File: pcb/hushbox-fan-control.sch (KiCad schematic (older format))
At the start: 23 parts, among them J1 Barrel_Jack_MountingPin, J2 Conn_01x15_Male, M1 Fan_Tacho_PWM, M2 Fan_Tacho_PWM, Q1 IRLML2520, Q2 IRLML2520, SW1 SW_SPST, U1 AMS1117-3.3, U2 ESP32-DevKit-V1, U3 DS18B20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

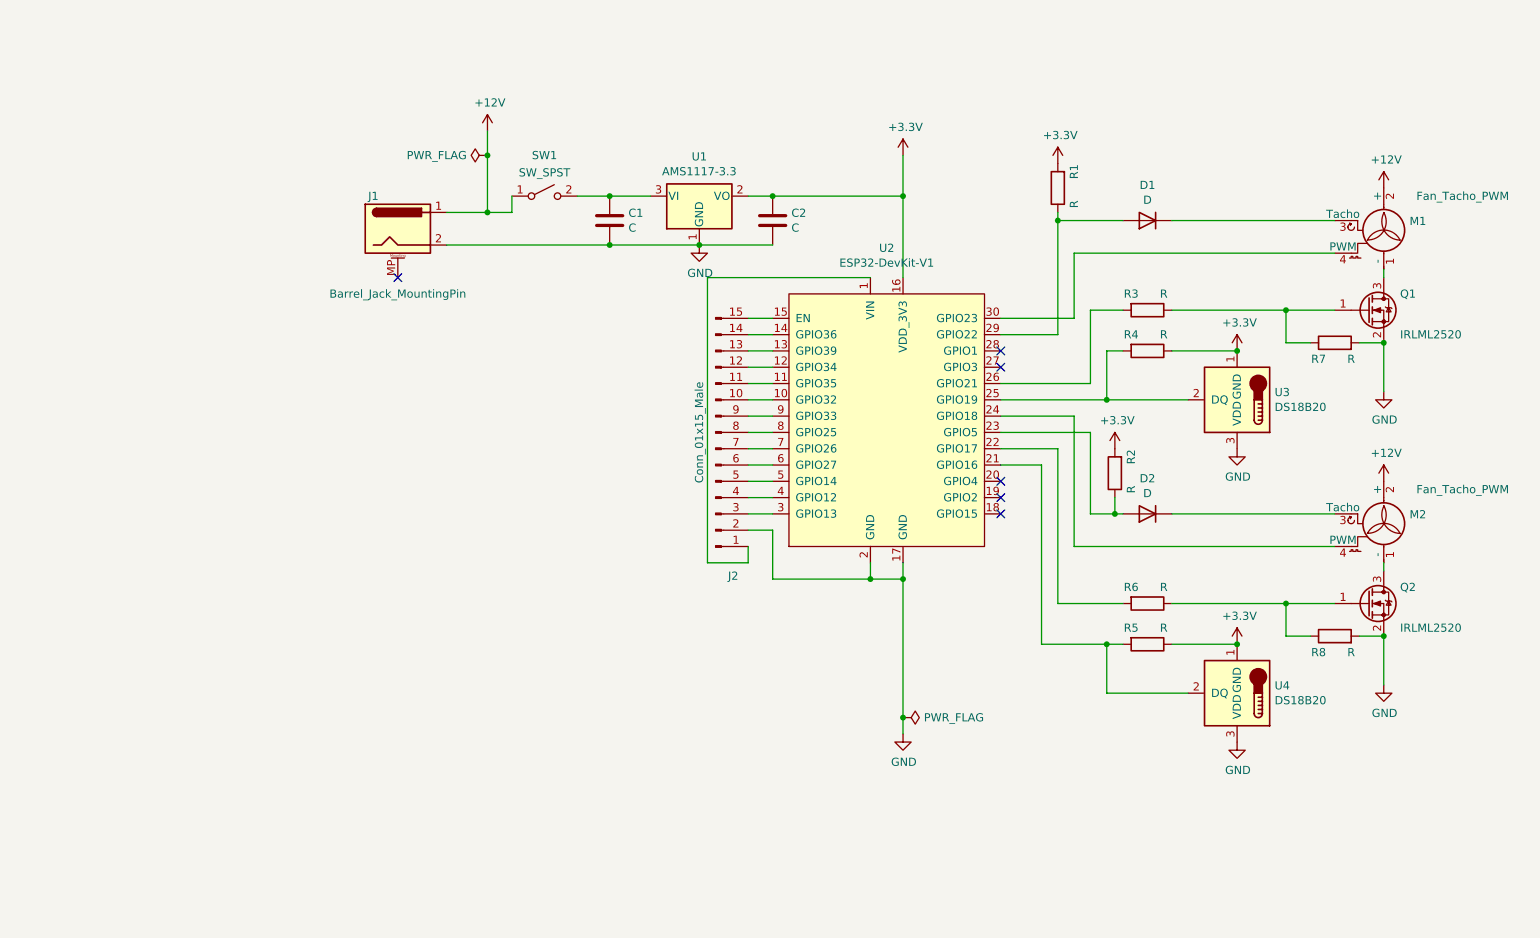
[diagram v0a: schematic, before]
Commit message: improve pcb to v1.1 with IR support
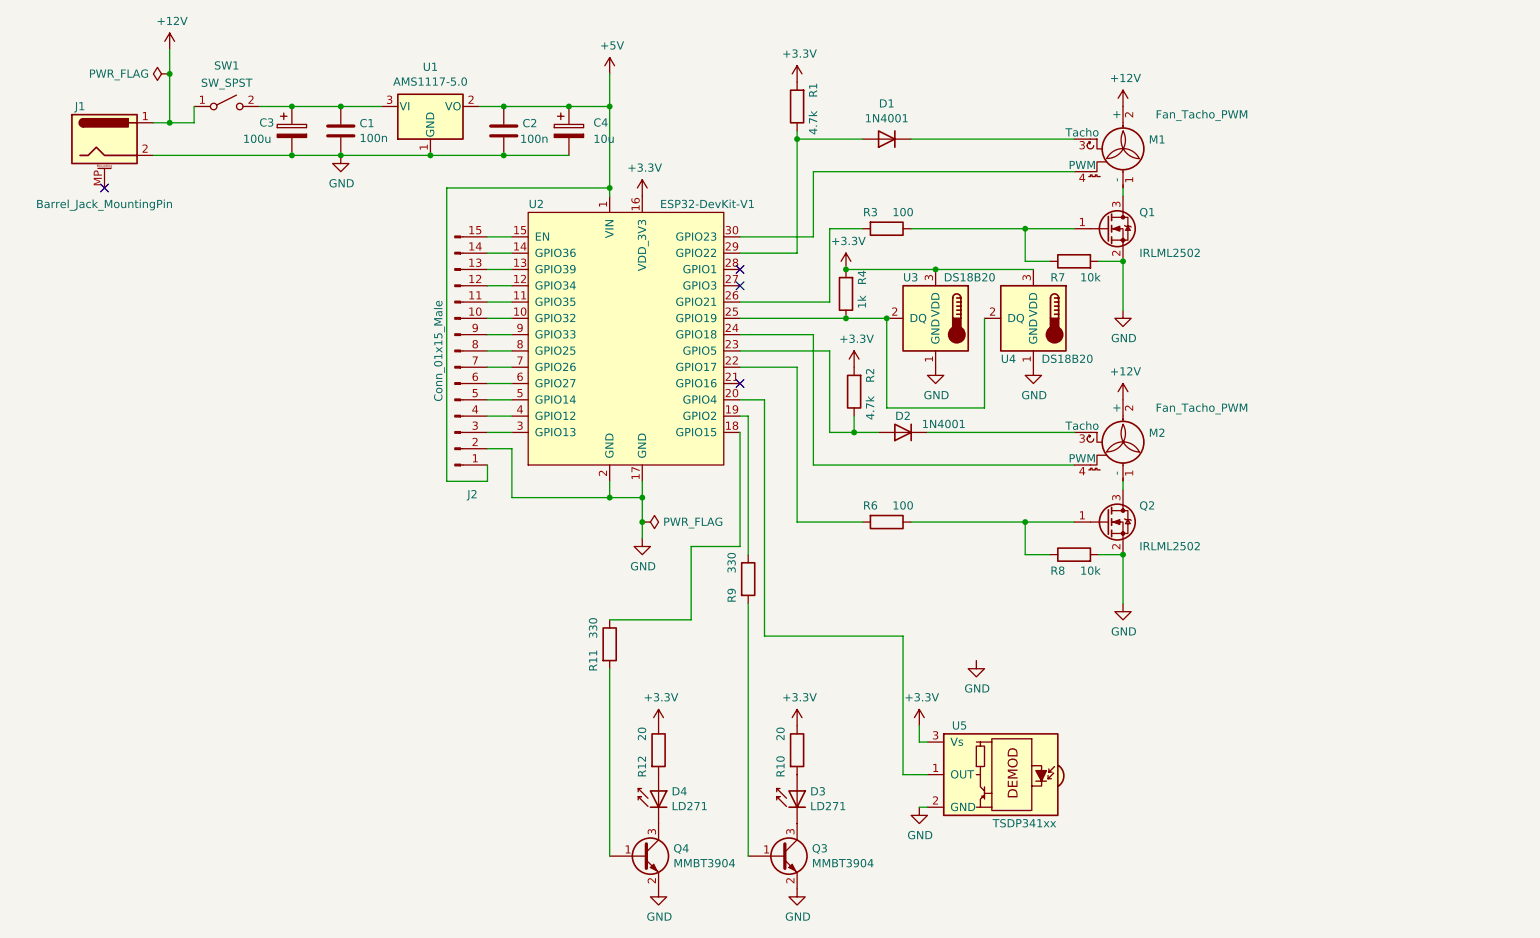
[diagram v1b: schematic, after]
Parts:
- removed R5: R, Resistor_SMD:R_0805_2012Metric_Pad1.20x1.40mm_HandSolder, symbol Device:R
- removed U1: AMS1117-3.3, Package_TO_SOT_SMD:SOT-223-3_TabPin2, symbol Regulator_Linear:AMS1117-3.3
- added C3: 100u, Capacitor_THT:CP_Radial_D8.0mm_P2.50mm, symbol Device:CP
- added C4: 10u, Capacitor_THT:CP_Radial_D5.0mm_P2.50mm, symbol Device:CP
- added D3, D4: LD271, Connector_JST:JST_XH_S2B-XH-A_1x02_P2.50mm_Horizontal, symbol LED:LD271
- added Q3, Q4: MMBT3904, Package_TO_SOT_SMD:SOT-23_Handsoldering, symbol Transistor_BJT:MMBT3904
- added R10, R12: 20, Resistor_SMD:R_0805_2012Metric_Pad1.20x1.40mm_HandSolder, symbol Device:R
- added R11, R9: 330, Resistor_SMD:R_0805_2012Metric_Pad1.20x1.40mm_HandSolder, symbol Device:R
- added U1: AMS1117-5.0, Package_TO_SOT_SMD:SOT-223-3_TabPin2, symbol Regulator_Linear:AMS1117-5.0
- added U5: TSDP341xx, Connector_JST:JST_XH_S3B-XH-A_1x03_P2.50mm_Horizontal, symbol Interface_Optical:TSDP341xx
- C1, C2: value C -> 100n
- D1, D2: value D -> 1N4001; footprint Diode_SMD:D_0805_2012Metric_Pad1.15x1.40mm_HandSolder -> Diode_SMD:D_SMA_Handsoldering
- J1: footprint Connector_BarrelJack:BarrelJack_Wuerth_6941xx301002 -> Connector_BarrelJack:BarrelJack_Horizontal
- Q1, Q2: value IRLML2520 -> IRLML2502; footprint Package_TO_SOT_SMD:SOT-23 -> Package_TO_SOT_SMD:SOT-23_Handsoldering
- R1, R2: value R -> 4.7k
- R3, R6: value R -> 100
- R4: value R -> 1k
- R7, R8: value R -> 10k
- SW1: footprint Connector_PinHeader_2.54mm:PinHeader_1x02_P2.54mm_Vertical -> Connector_PinSocket_2.54mm:PinSocket_1x02_P2.54mm_Vertical
- U3, U4: footprint Connector:FanPinHeader_1x03_P2.54mm_Vertical -> Connector_JST:JST_XH_B3B-XH-A_1x03_P2.50mm_Vertical
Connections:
- net +3V3: now also R4.2, U3.3 (VDD), U4.3 (VDD), R10.1, R12.1, U5.3 (Vs); no longer C2.1, R4.1, U3.1 (GND), U4.1 (GND)
- net GND: now also U3.1 (GND), U4.1 (GND), C3.2, C4.2, Q3.2 (E), Q4.2 (E), U1.1 (GND), U5.2 (GND); no longer U3.3 (VDD), U4.3 (VDD)
- net at C1.1, SW1.2 (B): now also C3.1, U1.3 (VI)
- net at U2.25 (GPIO19), U3.2 (DQ): now also R4.1, U4.2 (DQ); no longer R4.2
- net +5V: now reaches J2.1 (Pin_1), U2.1 (VIN)
- net +5V: now also C2.1, C4.1, U1.2 (VO)
- net at U2.18 (GPIO15): now also R11.1
- net at U2.19 (GPIO2): now also R9.1
- net at U2.20 (GPIO4): now also U5.1 (OUT)
- net at U2.21 (GPIO16): no longer U4.2 (DQ)
- new net: Q3.1 (B), R9.2
- new net: D3.1 (K), Q3.3 (C)
- new net: D3.2 (A), R10.2
- new net: Q4.1 (B), R11.2
- new net: D4.1 (K), Q4.3 (C)
- new net: D4.2 (A), R12.2
- no-connect marks 6 -> 4
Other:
- moved on the sheet: C1, C2, D1, D2, J1, J2, M1, M2, Q1, Q2, R1, R2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

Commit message: finalize PCB layout
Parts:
- added C?: 100u, Capacitor_THT:CP_Radial_D5.0mm_P2.50mm, symbol Device:CP
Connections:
- net at D1.2 (A), R1.1, U2.29 (GPIO22): now also C?.1
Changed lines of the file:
@@
 $EndComp
 NoConn ~ 1050 1900
+$Comp
+L Device:CP C?
+U 1 1 6003A0F3
+P 4900 1400
+F 0 "C?" H 5050 1450 50  0000 L CNN
+F 1 "100u" H 5050 1350 50  0000 L CNN
+F 2 "Capacitor_THT:CP_Radial_D5.0mm_P2.50mm" H 4938 1250 50  0001 C CNN
+F 3 "~" H 4900 1400 50  0001 C CNN
+	1    4900 1400
+	-1   0    0    1
+$EndComp
+Wire Wire Line
+	4900 1550 4900 1600
+Wire Wire Line
+	4900 1600 5300 1600
 $EndSCHEMATC
